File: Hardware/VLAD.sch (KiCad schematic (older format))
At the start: 16 parts

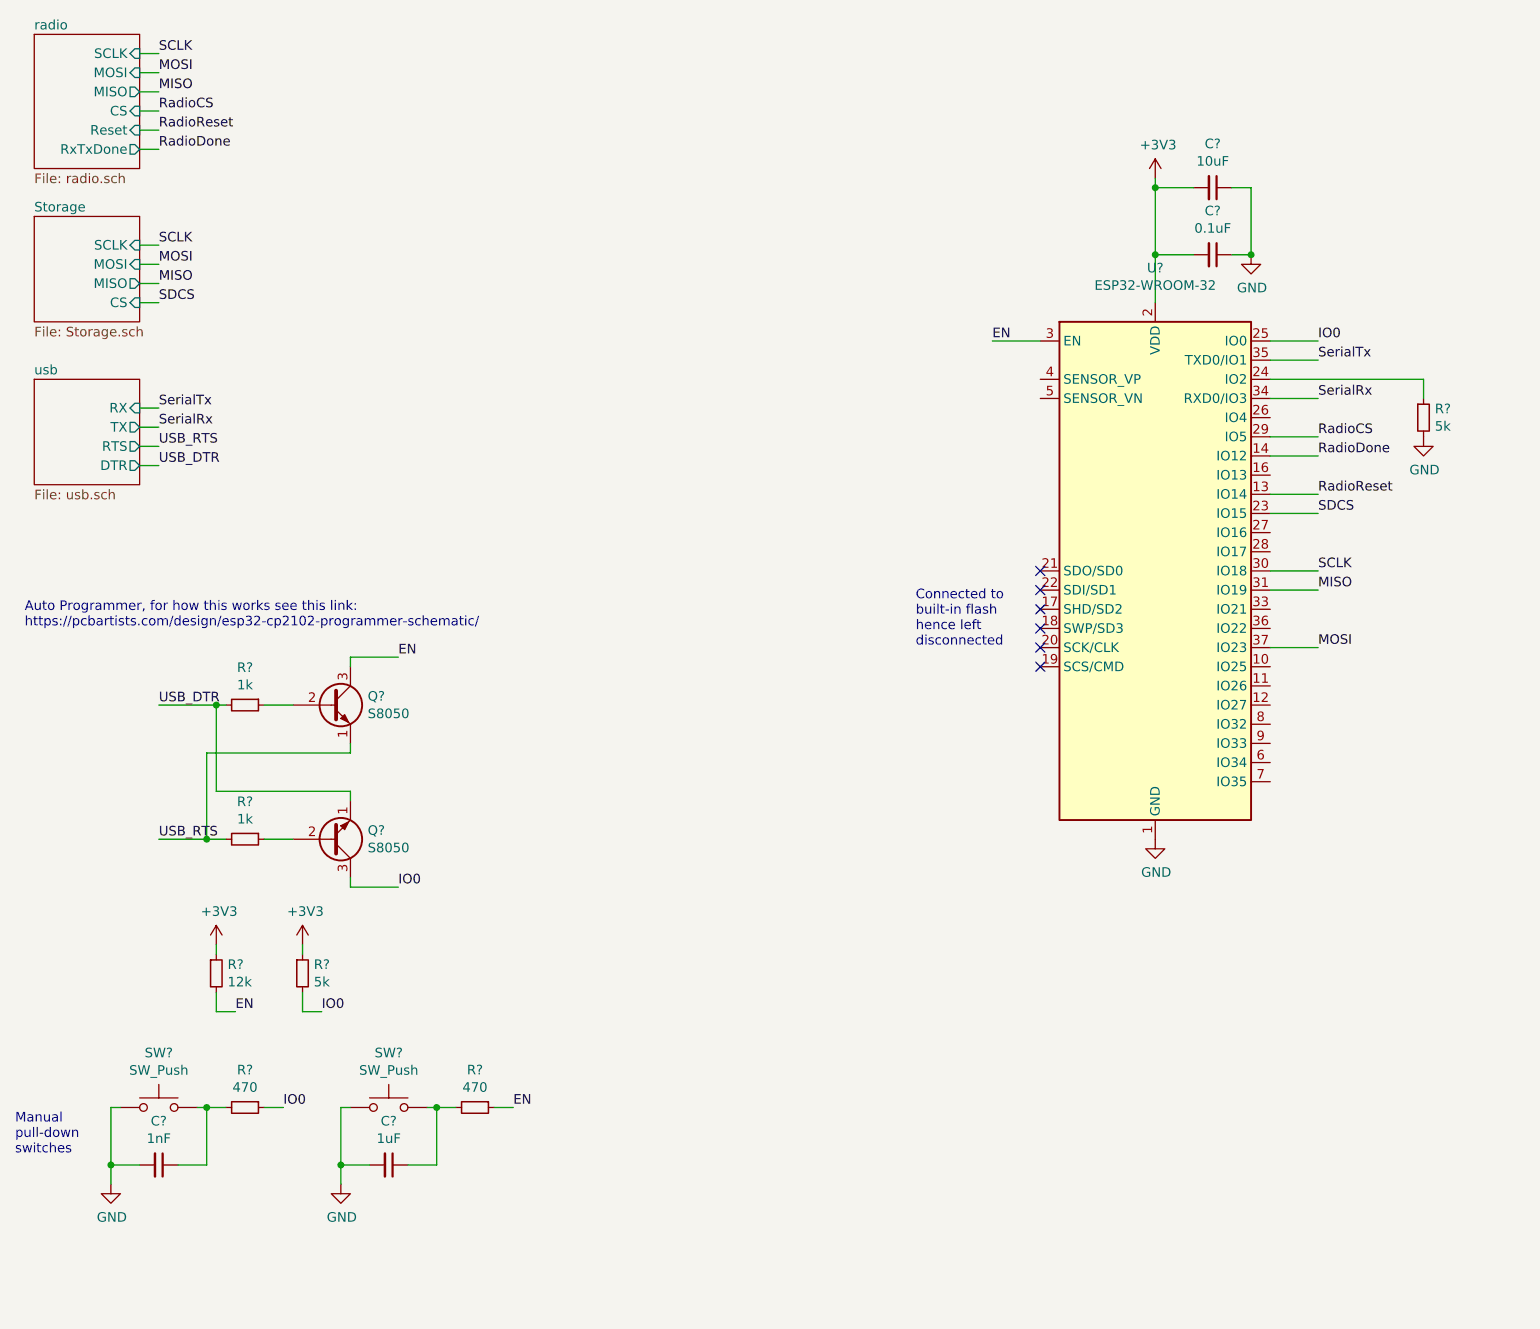
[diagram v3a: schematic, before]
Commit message: Added connector to program using external FTDI chip
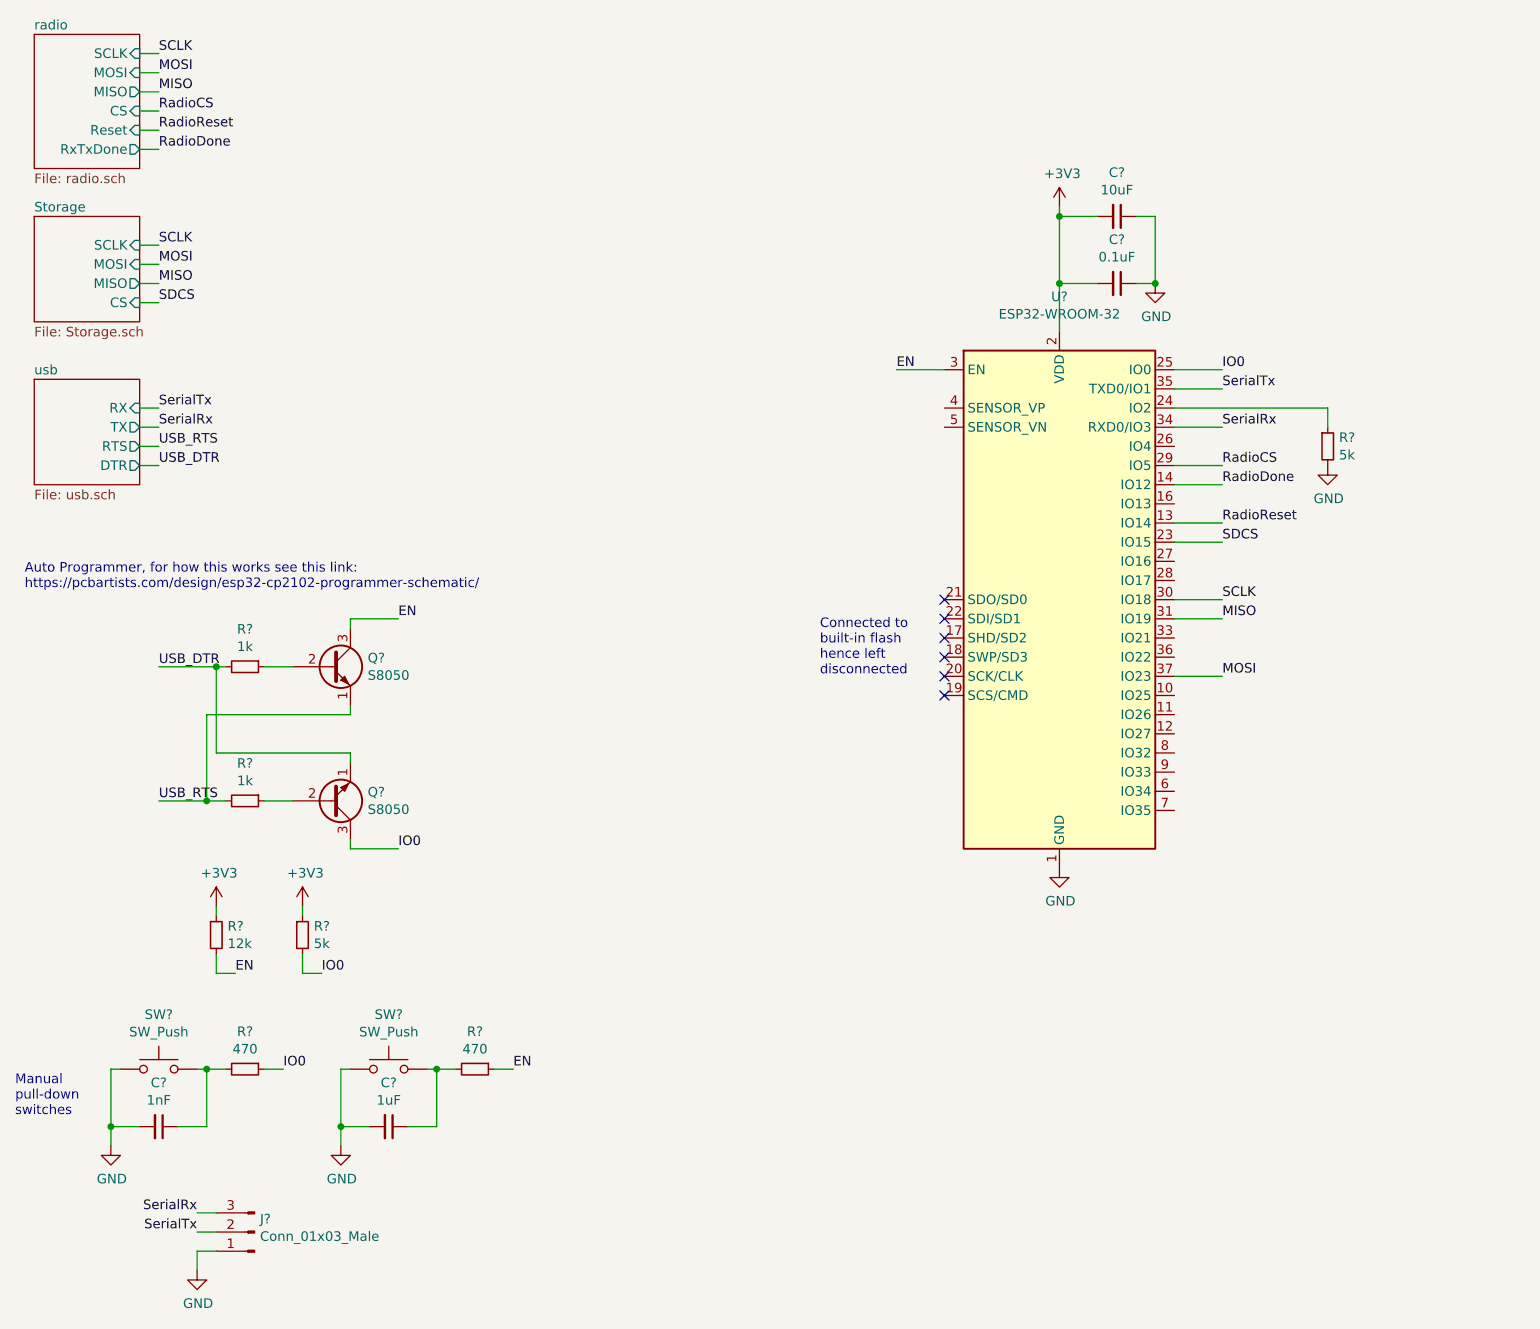
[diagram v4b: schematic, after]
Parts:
- added J?: Conn_01x03_Male, symbol Connector:Conn_01x03_Male
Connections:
- net GND: now also J?.1 (Pin_1)
- net SerialRx: now also J?.3 (Pin_3)
- net SerialTx: now also J?.2 (Pin_2)
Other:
- moved on the sheet: C?, Q?, R?, SW?, U?

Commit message: Added connectors to SPI pins for debugging
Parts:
- added J?: Conn_01x04_Male, symbol Connector:Conn_01x04_Male
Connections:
- net GND: now also J?.1 (Pin_1)
- net MISO: now also J?.2 (Pin_2)
- net MOSI: now also J?.3 (Pin_3)
- net SCLK: now also J?.4 (Pin_4)
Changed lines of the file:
@@
+	1    0    0    -1
+$EndComp
+$Comp
+L Connector:Conn_01x04_Male J?
+U 1 1 60A5081B
+P 2700 1100
+F 0 "J?" H 2672 982 50  0000 R CNN
+F 1 "Conn_01x04_Male" H 2672 1073 50  0000 R CNN
+F 2 "" H 2700 1100 50  0001 C CNN
+F 3 "~" H 2700 1100 50  0001 C CNN
+	1    2700 1100
+	-1   0    0    1
+$EndComp
+Wire Wire Line
+	2350 900  2500 900
+Wire Wire Line
+	2350 1000 2500 1000
+Wire Wire Line
+	2350 1100 2500 1100
+Text Label 2350 900  0    50   ~ 0
+SCLK
+Text Label 2350 1000 0    50   ~ 0
+MOSI
+Text Label 2350 1100 0    50   ~ 0
+MISO
+Wire Wire Line
+	2500 1200 2400 1200
+Wire Wire Line
+	2400 1200 2400 1300
+$Comp
+L power:GND #PWR?
+U 1 1 60A626D9
+P 2400 1300
+F 0 "#PWR?" H 2400 1050 50  0001 C CNN
+F 1 "GND" H 2405 1127 50  0000 C CNN
+F 2 "" H 2400 1300 50  0001 C CNN
+F 3 "" H 2400 1300 50  0001 C CNN
+	1    2400 1300
 	1    0    0    -1
 $EndComp
